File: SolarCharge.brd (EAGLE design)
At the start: 63 x 63 mm, 8 parts

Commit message: Improve GND
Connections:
- net N$2 renamed GND
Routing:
- net GND: vias 4 -> 23
- added copper zone on layer 1, net GND
- added copper zone on layer 16, net GND
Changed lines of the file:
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@@
 <?xml version="1.0" encoding="utf-8"?>
 <!DOCTYPE eagle SYSTEM "eagle.dtd">
-<eagle version="9.1.0">
+<eagle version="7.7.0">
 <drawing>
 <settings>
@@
 <param name="dpMaxLengthDifference" value="10mm"/>
 <param name="dpGapFactor" value="2.5"/>
+<param name="checkGrid" value="0"/>
 <param name="checkAngle" value="0"/>
 <param name="checkFont" value="1"/>
 <param name="checkRestrict" value="1"/>
-<param name="checkStop" value="0"/>
-<param name="checkValues" value="0"/>
-<param name="checkNames" value="1"/>
-<param name="checkWireStubs" value="1"/>
-<param name="checkPolygonWidth" value="0"/>
 <param name="useDiameter" value="13"/>
 <param name="maxErrors" value="50"/>
@@
 <wire x1="33.5" y1="16.94" x2="33.5" y2="24.5" width="0.4064" layer="1"/>
 </signal>
-<signal name="N$2">
+<signal name="GND">
 <contactref element="U$1" pad="P$2"/>
 <contactref element="J2" pad="GROUND"/>
@@
 <wire x1="22.432" y1="40.068" x2="22.432" y2="45.93" width="0.4064" layer="16"/>
 <via x="22.432" y="45.93" extent="1-16" drill="0.35"/>
+<polygon width="0.6096" layer="1">
+<vertex x="19.75" y="-0.25"/>
+<vertex x="20" y="-0.25" curve="90"/>
+<vertex x="51.75" y="31.5" curve="90"/>
+<vertex x="20.5" y="62.75"/>
+<vertex x="20.25" y="62.75" curve="90"/>
+<vertex x="-11" y="31.5"/>
+<vertex x="-11" y="30.5" curve="90"/>
+</polygon>
+<polygon width="0.6096" layer="16">
+<vertex x="20.5" y="-0.25"/>
+<vertex x="20.75" y="-0.25" curve="90"/>
+<vertex x="52" y="31"/>
+<vertex x="52" y="31.5" curve="90"/>
+<vertex x="20.75" y="62.75"/>
+<vertex x="20.5" y="62.75" curve="90"/>
+<vertex x="-11" y="31.25" curve="90"/>
+</polygon>
+<via x="29" y="34.75" extent="1-16" drill="0.35"/>
+<via x="29" y="28.5" extent="1-16" drill="0.35"/>
+<via x="12.5" y="54.5" extent="1-16" drill="0.35"/>
+<via x="8.75" y="48.25" extent="1-16" drill="0.35"/>
+<via x="12" y="43.25" extent="1-16" drill="0.35"/>
+<via x="8" y="40" extent="1-16" drill="0.35"/>
+<via x="31.5" y="42.25" extent="1-16" drill="0.35"/>
+<via x="30.75" y="53.75" extent="1-16" drill="0.35"/>
+<via x="27.25" y="45.25" extent="1-16" drill="0.35"/>
+<via x="31.25" y="17.25" extent="1-16" drill="0.35"/>
+<via x="29.25" y="8.5" extent="1-16" drill="0.35"/>
+<via x="24.5" y="11.25" extent="1-16" drill="0.35"/>
+<via x="20.25" y="9.75" extent="1-16" drill="0.35"/>
+<via x="14.5" y="9.25" extent="1-16" drill="0.35"/>
+<via x="16" y="12" extent="1-16" drill="0.35"/>
+<via x="7.5" y="21.75" extent="1-16" drill="0.35"/>
+<via x="11.25" y="24.25" extent="1-16" drill="0.35"/>
+<via x="15.75" y="38" extent="1-16" drill="0.35"/>
+<via x="15" y="14.75" extent="1-16" drill="0.35"/>
 </signal>
 <signal name="N$3">
@@
 </signal>
 </signals>
-<mfgpreviewcolors>
-<mfgpreviewcolor name="soldermaskcolor" color="0xC8008000"/>
-<mfgpreviewcolor name="silkscreencolor" color="0xFFFEFEFE"/>
-<mfgpreviewcolor name="backgroundcolor" color="0xFF282828"/>
-<mfgpreviewcolor name="coppercolor" color="0xFFFFBF00"/>
-<mfgpreviewcolor name="substratecolor" color="0xFF786E46"/>
-</mfgpreviewcolors>
 </board>
 </drawing>

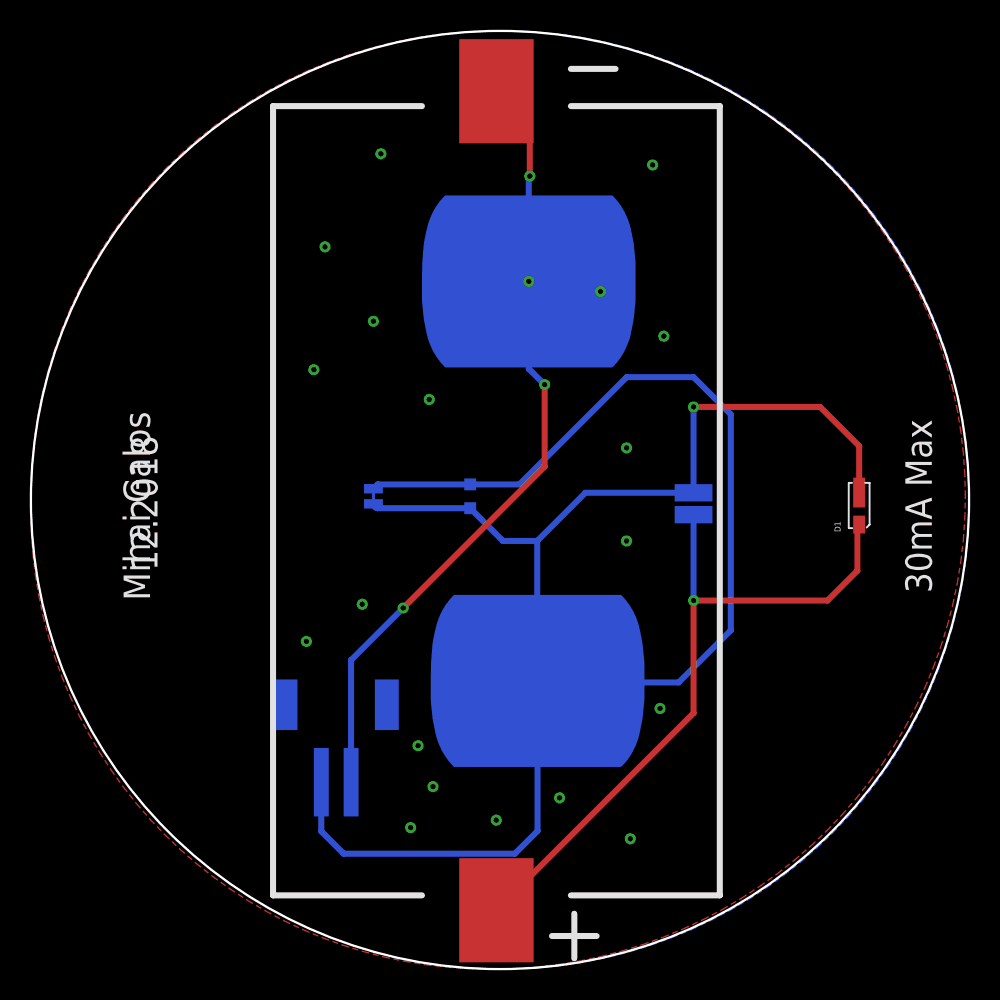
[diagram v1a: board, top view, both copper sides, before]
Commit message: Add logos, recenter
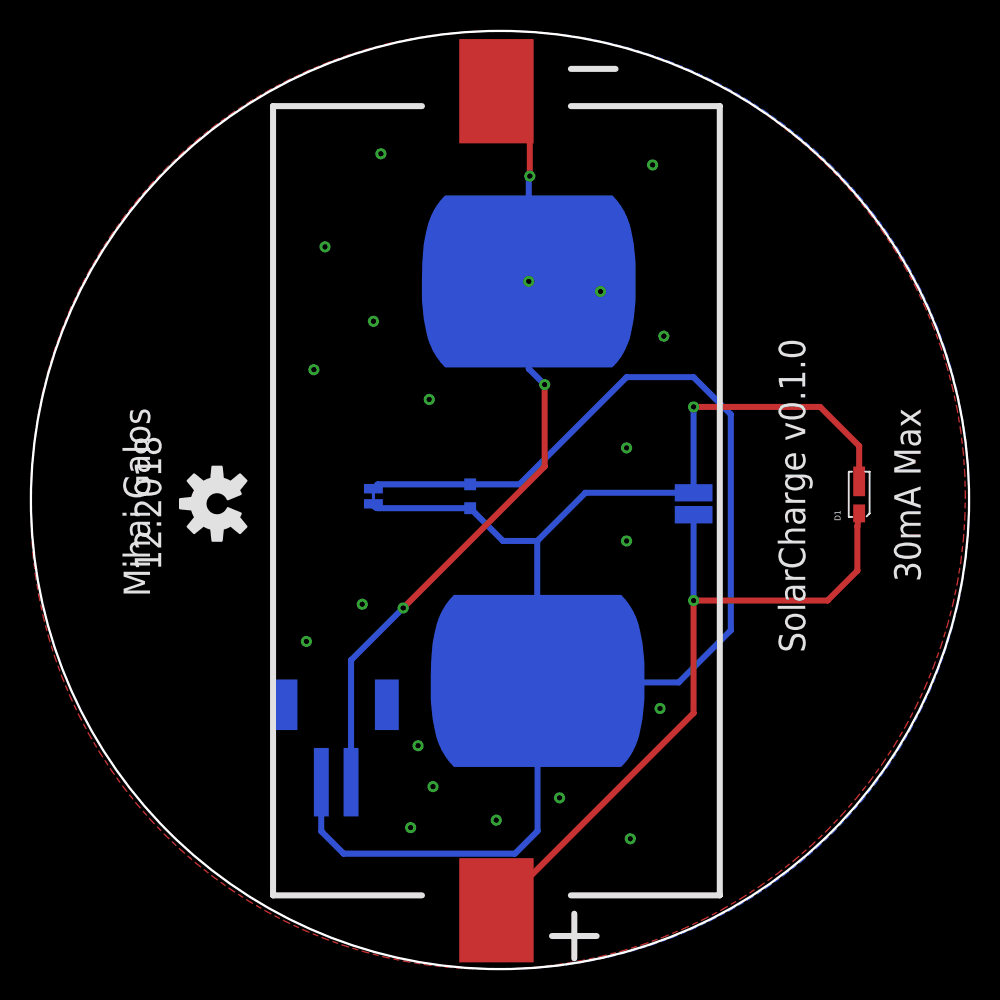
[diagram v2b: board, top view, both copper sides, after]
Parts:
- added LOGO1: OSHW-LOGOM, Spark:OSHW-LOGO-M
- moved D1 0.75 mm to (44.6, 30.4)
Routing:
- net N$3: track 54.4 -> 53.6 mm
- net N$1: track 47.0 -> 47.7 mm
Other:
- board text added: "SolarCharge v0.1.0"
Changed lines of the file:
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@@
 <wire x1="32.5" y1="9.5" x2="32.5" y2="12.5" width="0.4064" layer="22"/>
 <wire x1="31" y1="50" x2="34" y2="50" width="0.4064" layer="22"/>
-<text x="49.5" y="25" size="1.778" layer="21" rot="R90">30mA Max</text>
-<text x="-3" y="24.5" size="1.778" layer="21" rot="R90">Mihai Galos
+<text x="48.75" y="25.75" size="1.778" layer="21" rot="R90">30mA Max</text>
+<text x="-3" y="24.75" size="1.778" layer="21" rot="R90">Mihai Galos
 </text>
-<text x="-2.5" y="26.5" size="1.778" layer="21" rot="R90">12.2018</text>
+<text x="-2.25" y="26.5" size="1.778" layer="21" rot="R90">12.2018</text>
 <text x="9.5" y="38" size="1.016" layer="22" rot="MR270">Fallback to 0603 led.</text>
 <wire x1="10.5" y1="35.5" x2="10.5" y2="26.5" width="0.4064" layer="22" style="shortdash"/>
@@
 <wire x1="21.5" y1="35.5" x2="10.5" y2="35.5" width="0.4064" layer="22" style="shortdash"/>
 <circle x="20.5" y="31.25" radius="31.5" width="0.1524" layer="20"/>
+<text x="41" y="21" size="1.778" layer="21" rot="R90">SolarCharge v0.1.0</text>
 </plain>
 <attributes>
@@
 </autorouter>
 <elements>
-<element name="D1" library="Wurth_Elektronik_Optoelectronics_rev15c" package="WL-SWTP_3014" value="" x="44.62" y="29.6" rot="R90"/>
+<element name="D1" library="Wurth_Elektronik_Optoelectronics_rev15c" package="WL-SWTP_3014" value="" x="44.62" y="30.35" rot="R90"/>
 <element name="U$1" library="solar_panel_53_30" package="SOLAR_CELL_53_30" value="SOLAR_CELL_53_30" x="5.26" y="4.7"/>
 <element name="J1" library="SparkFun-Connectors" package="STARBOARD_GROUND_WIDE" value="" x="15.91" y="19.1" rot="MR90"/>
@@
 <element name="SJ1" library="SparkFun-Passives" package="SJ_2S-TRACE" value="SOLDERJUMPER-OLDTRACE" x="12" y="31.5" rot="MR90"/>
 <element name="CN1" library="lio" package="JST-PH-2-SMT-RA" value="" x="9.5" y="16" rot="MR0"/>
+<element name="LOGO1" library="Spark" package="OSHW-LOGO-M" value="OSHW-LOGOM" x="1.5" y="31" rot="R90"/>
 </elements>
 <signals>
@@
 <contactref element="D1" pad="2"/>
 <contactref element="J3" pad="1"/>
-<wire x1="44.62" y1="29.6" x2="44.5" y2="29.48" width="0.4064" layer="1"/>
+<wire x1="44.62" y1="30.35" x2="44.5" y2="29.48" width="0.4064" layer="1"/>
 <wire x1="44.5" y1="29.48" x2="44.5" y2="26.5" width="0.4064" layer="1"/>
 <wire x1="44.5" y1="26.5" x2="42.5" y2="24.5" width="0.4064" layer="1"/>
@@
 <contactref element="D1" pad="1"/>
 <contactref element="J3" pad="2"/>
-<wire x1="44.62" y1="31.75" x2="44.62" y2="34.88" width="0.4064" layer="1"/>
+<wire x1="44.62" y1="32.5" x2="44.62" y2="34.88" width="0.4064" layer="1"/>
 <wire x1="42" y1="37.5" x2="33.5" y2="37.5" width="0.4064" layer="1"/>
 <via x="33.5" y="37.5" extent="1-16" drill="0.35"/>

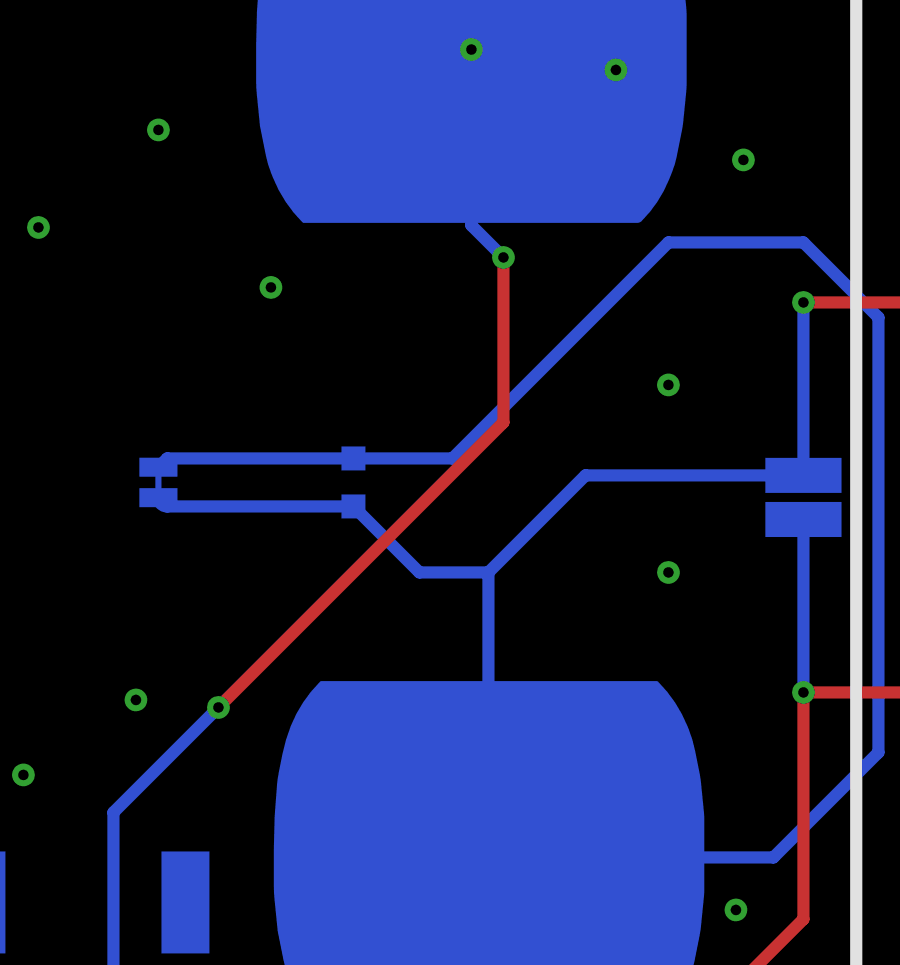
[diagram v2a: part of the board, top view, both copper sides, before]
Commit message: Add solar panel info
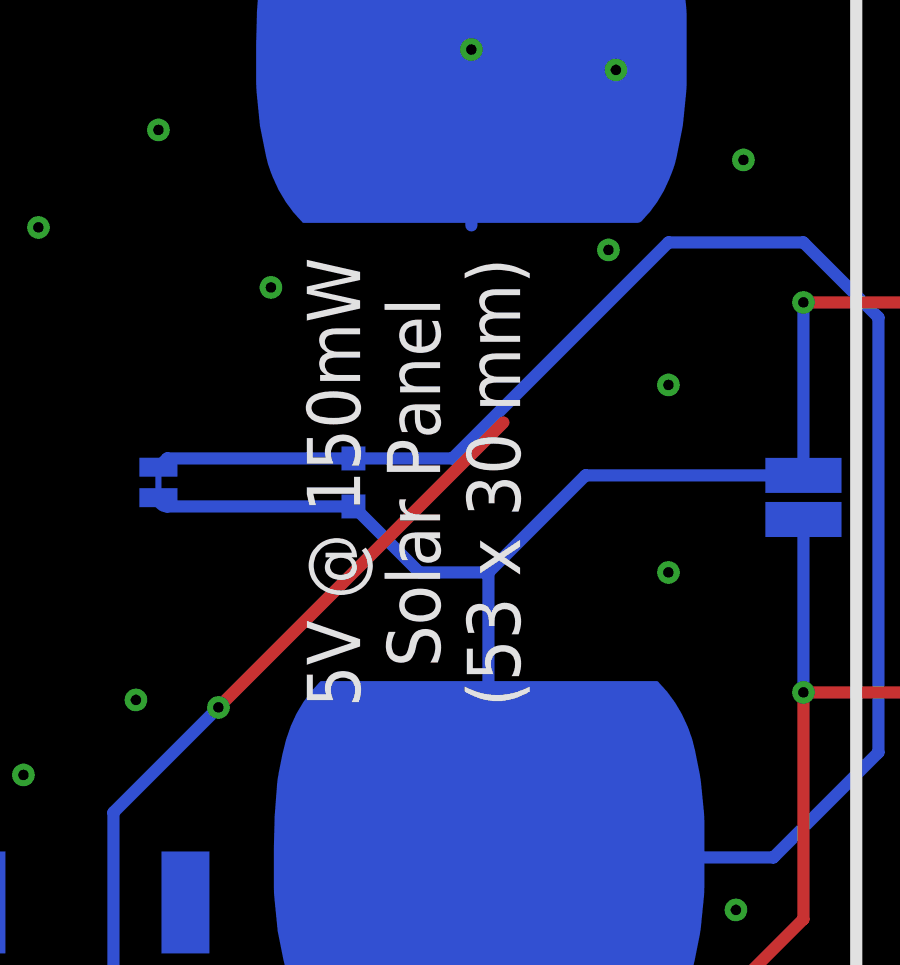
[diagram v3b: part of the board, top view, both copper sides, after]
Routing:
- net GND: track 53.2 -> 46.2 mm
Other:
- board text added: "5V @ 150mW Solar Panel (53 x 30 mm)"
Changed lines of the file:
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@@
 <circle x="20.5" y="31.25" radius="31.5" width="0.1524" layer="20"/>
 <text x="41" y="21" size="1.778" layer="21" rot="R90">SolarCharge v0.1.0</text>
+<text x="20.5" y="31.5" size="1.778" layer="21" rot="R90" align="center">5V @ 150mW
+Solar Panel
+(53 x 30 mm)</text>
 </plain>
 <attributes>
@@
 <via x="14" y="24" extent="1-16" drill="0.35"/>
 <wire x1="14" y1="24" x2="23.5" y2="33.5" width="0.4064" layer="1"/>
-<wire x1="23.5" y1="33.5" x2="23.5" y2="39" width="0.4064" layer="1"/>
-<via x="23.5" y="39" extent="1-16" drill="0.35"/>
-<wire x1="23.5" y1="39" x2="22.432" y2="40.068" width="0.4064" layer="16"/>
+<via x="27" y="39.25" extent="1-16" drill="0.35"/>
 <wire x1="22.432" y1="40.068" x2="22.432" y2="45.93" width="0.4064" layer="16"/>
 <via x="22.432" y="45.93" extent="1-16" drill="0.35"/>

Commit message: Realign to center
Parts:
- moved LOGO1 0.50 mm to (1.50, 31.5)
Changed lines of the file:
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@@
 <wire x1="31" y1="50" x2="34" y2="50" width="0.4064" layer="22"/>
 <text x="48.75" y="25.75" size="1.778" layer="21" rot="R90">30mA Max</text>
-<text x="-3" y="24.75" size="1.778" layer="21" rot="R90">Mihai Galos
+<text x="-3" y="23.75" size="1.778" layer="21" rot="R90">Mihai Galos
 </text>
 <text x="-2.25" y="26.5" size="1.778" layer="21" rot="R90">12.2018</text>
@@
 <wire x1="21.5" y1="35.5" x2="10.5" y2="35.5" width="0.4064" layer="22" style="shortdash"/>
 <circle x="20.5" y="31.25" radius="31.5" width="0.1524" layer="20"/>
-<text x="41" y="21" size="1.778" layer="21" rot="R90">SolarCharge v0.1.0</text>
+<text x="41" y="18.75" size="1.778" layer="21" rot="R90">SolarCharge v0.1.0</text>
 <text x="20.5" y="31.5" size="1.778" layer="21" rot="R90" align="center">5V @ 150mW
 Solar Panel
@@
 <element name="SJ1" library="SparkFun-Passives" package="SJ_2S-TRACE" value="SOLDERJUMPER-OLDTRACE" x="12" y="31.5" rot="MR90"/>
 <element name="CN1" library="lio" package="JST-PH-2-SMT-RA" value="" x="9.5" y="16" rot="MR0"/>
-<element name="LOGO1" library="Spark" package="OSHW-LOGO-M" value="OSHW-LOGOM" x="1.5" y="31" rot="R90"/>
+<element name="LOGO1" library="Spark" package="OSHW-LOGO-M" value="OSHW-LOGOM" x="1.5" y="31.5" rot="R90"/>
 </elements>
 <signals>

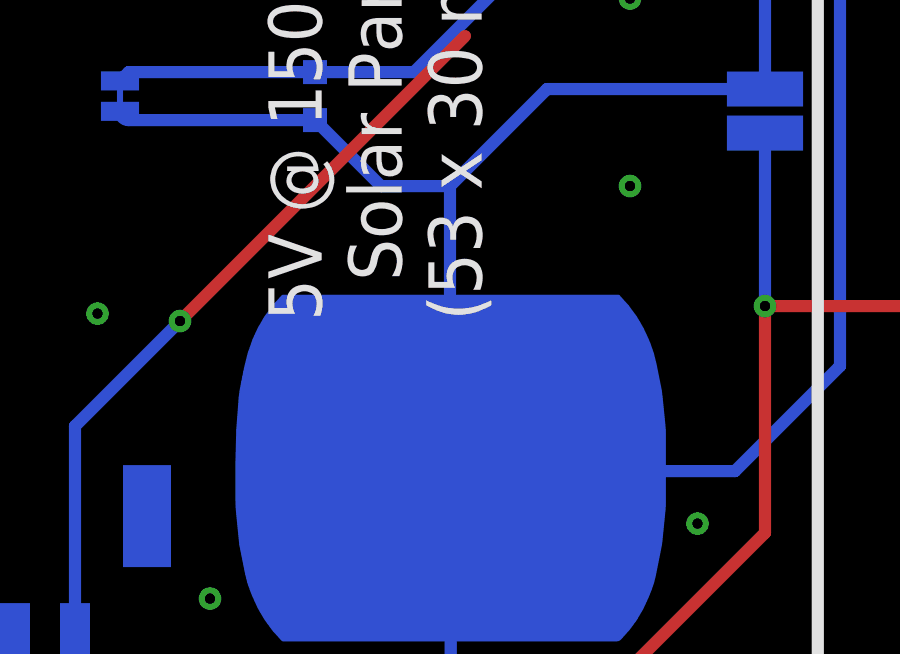
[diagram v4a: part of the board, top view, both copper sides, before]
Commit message: Correct stray signal
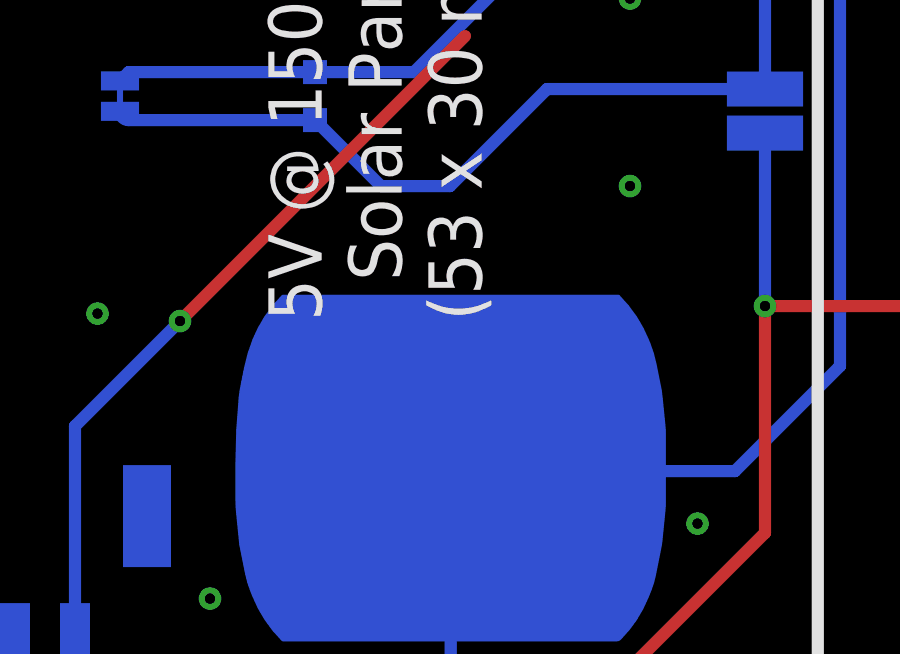
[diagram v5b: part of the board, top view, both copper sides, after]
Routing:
- net N$3: track 53.6 -> 44.2 mm
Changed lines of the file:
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@@
 <?xml version="1.0" encoding="utf-8"?>
 <!DOCTYPE eagle SYSTEM "eagle.dtd">
-<eagle version="7.7.0">
+<eagle version="9.1.0">
 <drawing>
 <settings>
 <setting alwaysvectorfont="no"/>
+<setting keepoldvectorfont="yes"/>
 <setting verticaltext="up"/>
 </settings>
@@
 <param name="dpMaxLengthDifference" value="10mm"/>
 <param name="dpGapFactor" value="2.5"/>
-<param name="checkGrid" value="0"/>
 <param name="checkAngle" value="0"/>
 <param name="checkFont" value="1"/>
 <param name="checkRestrict" value="1"/>
+<param name="checkStop" value="0"/>
+<param name="checkValues" value="0"/>
+<param name="checkNames" value="1"/>
+<param name="checkWireStubs" value="1"/>
+<param name="checkPolygonWidth" value="0"/>
 <param name="useDiameter" value="13"/>
 <param name="maxErrors" value="50"/>
@@
 <wire x1="33.5" y1="31.735" x2="26.235" y2="31.735" width="0.4064" layer="16"/>
 <wire x1="26.235" y1="31.735" x2="23" y2="28.5" width="0.4064" layer="16"/>
-<wire x1="23" y1="28.5" x2="23" y2="19.122" width="0.4064" layer="16"/>
 <contactref element="SJ1" pad="1"/>
 <contactref element="R1" pad="1"/>
@@
 </signal>
 </signals>
+<mfgpreviewcolors>
+<mfgpreviewcolor name="soldermaskcolor" color="0xC8008000"/>
+<mfgpreviewcolor name="silkscreencolor" color="0xFFFEFEFE"/>
+<mfgpreviewcolor name="backgroundcolor" color="0xFF282828"/>
+<mfgpreviewcolor name="coppercolor" color="0xFFFFBF00"/>
+<mfgpreviewcolor name="substratecolor" color="0xFF786E46"/>
+</mfgpreviewcolors>
 </board>
 </drawing>
